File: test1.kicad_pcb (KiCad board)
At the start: 2 copper layers, 228.6 x 81.7 mm, 115 parts, among them J1 AVR-ISP-6, K1 KEYSW, K10 KEYSW, K11 KEYSW, K12 KEYSW, K13 KEYSW, K14 KEYSW, K15 KEYSW, K16 KEYSW, K17 KEYSW, K18 KEYSW, K19 KEYSW, K2 KEYSW, K20 KEYSW, K21 KEYSW, K22 KEYSW, K23 KEYSW, K24 KEYSW, K25 KEYSW, K26 KEYSW, K27 KEYSW, K28 KEYSW, K29 KEYSW, K3 KEYSW, K30 KEYSW, K31 KEYSW, K32 KEYSW, K33 KEYSW, K34 KEYSW, K35 KEYSW, K36 KEYSW, K37 KEYSW, K38 KEYSW, K39 KEYSW, K4 KEYSW, K40 KEYSW, K41 KEYSW, K42 KEYSW, K43 KEYSW, K44 KEYSW, K45 KEYSW, K46 KEYSW, K47 KEYSW, K48 KEYSW, K5 KEYSW, K6 KEYSW, K7 KEYSW, K8 KEYSW, K9 KEYSW, SW1 SW_PUSH, U1 ATMEGA32U2, Y1 XTAL

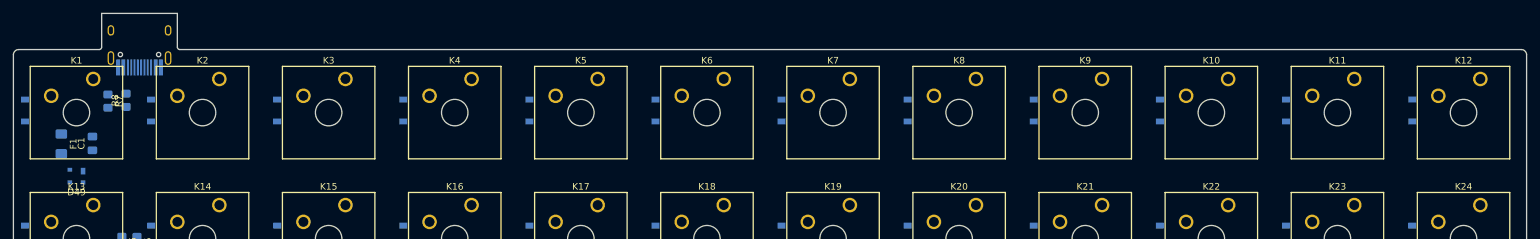
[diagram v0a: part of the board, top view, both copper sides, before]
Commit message: changed usb connector to be flush with edge of keys
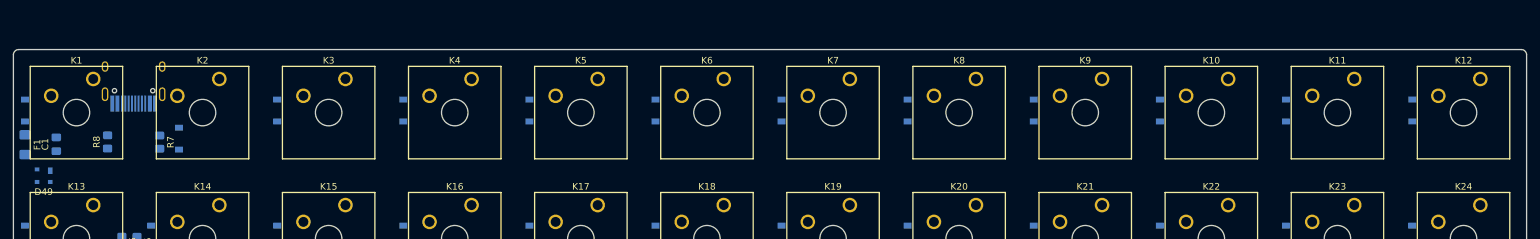
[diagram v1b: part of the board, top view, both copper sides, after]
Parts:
- moved R7 9.97 mm to (53.8, 37.7)
- moved R8 6.88 mm to (46.0, 37.7)
- moved D2 6.00 mm to (56.8, 37.2)
- moved USB1 5.53 mm to (49.9, 23.7)
- moved C1 5.46 mm to (38.2, 38.1)
- moved F1 5.46 mm to (33.5, 38.1)
- moved D49 4.95 mm to (36.3, 42.8)
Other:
- board size 228.6 x 81.7 mm -> 228.6 x 76.3 mm
